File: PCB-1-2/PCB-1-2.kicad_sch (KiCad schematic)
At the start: 79 parts, among them J1 Bus_PCI_Express_x8, J2 ST STDC14 (Debug Connector), J3 USB4105-GF-A, U1 LTC1298IS8_PBF, U10 INA827AIDGKR, U11 LTC1250CS8-PBF, U12 REF3425MDBVTEP, U13 HI-3585APQI, U2 LTC1451IS8-PBF, U3 HI-3110PSIF, U4 FT231XS-R, U5 STM32F103RBT6, U6 STWD100YNXWY3F, U7 ADP7104ACPZ-R7 (v3.3), U8 OPA2187IDGKR, U9 ADP7104ACPZ-R7 (5v), Y1 8MHz Crystal

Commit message: Moved a few things around and shrunk the overall schematic size
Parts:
- removed D1, D2: LED, symbol Device:LED
- removed R11, R12: R, symbol Device:R
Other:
- moved on the sheet: U3

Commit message: Updated Schematic & organized the board layout
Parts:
- added C32, C35, C36: 47uF, Capacitor_SMD:C_0805_2012Metric, symbol Device:C
- added C33, C34, C37, C38: 0.1uF, Capacitor_SMD:C_0805_2012Metric, symbol Device:C
- added C39, C44: .001uF, Capacitor_SMD:C_0805_2012Metric, symbol Device:C
- added C40, C43: .01uF, Capacitor_SMD:C_0805_2012Metric, symbol Device:C
- added C41, C42: .1uF, Capacitor_SMD:C_0805_2012Metric, symbol Device:C
- added C45, C46: 10pF, Capacitor_SMD:C_0805_2012Metric, symbol Device:C
- added D1: PWR_LED, LED_SMD:LED_0805_2012Metric, symbol Device:LED
- added R1, R29: 22, Resistor_SMD:R_0805_2012Metric, symbol Device:R
- added R11: 10k, Resistor_SMD:R_0805_2012Metric, symbol Device:R
- added R12: 1.5Meg, Resistor_SMD:R_0805_2012Metric, symbol Device:R
- added R27: 4.7k, Resistor_SMD:R_0805_2012Metric, symbol Device:R
- added R28: 2k, Resistor_SMD:R_0805_2012Metric, symbol Device:R
- added Y2: ABM8-24.000MHz-10-B1U-T, SDII LIB:XTAL_ABM8-24.000MHz-10-B1U-T, symbol ABM8-24MHz (Crystal):ABM8-24.000MHz-10-B1U-T
- C21, C22, C23, C24, C25, C26, C27, C28, C29, C30, C31: footprint (none) -> Capacitor_SMD:C_0805_2012Metric
- FB2: footprint (none) -> Inductor_SMD:L_0805_2012Metric
- R13, R14, R15, R16, R17, R18, R19, R2, R20, R21, R22, R23, R24, R25, R26, R3, R4: footprint (none) -> Resistor_SMD:R_0805_2012Metric
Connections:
- net SPI2_CS is gone; now on net SPI1_CS: U1.1 (*CS/SHDN), U13.9 (~{CS}), U2.3 (*CS/LD), U5.33 (PB12)
- net +3.3V: now also C32.1, C33.1, C38.2, C42.2, C43.2, C44.2, R11.1, R28.1
- net +5V: now also C34.1, C35.1, C39.1, C40.1, C41.1
- net -5V: now also C36.2, C37.2
- net GND: now also C27.2, J3.SH1 (SHELL_GND), J3.SH2 (SHELL_GND__1), J3.SH3 (SHELL_GND__2), J3.SH4 (SHELL_GND__3), C32.2, C33.2, C34.2, C35.2, C36.1, C37.1, C38.1, C39.2, C40.2, C41.2, C42.1, C43.1, C44.1, C45.2, C46.2, D1.1 (K), R1.2, Y2.2 (GND), Y2.4 (GND__1); no longer U13.17 (GND)
- net MCU_NRST: now also R27.1; no longer U6.1 (*WDO)
- net SPI1_CS: now also U3.16 (*CS)
- net SPI1_MISO: now also U3.15 (SO)
- net SPI1_MOSI: now also U3.14 (SI)
- net SPI1_SCK: now also U3.13 (SCK)
- net SWCLK: now also R29.2; no longer J2.06 (SWCLK)
- net 429_RFLAG: now reaches U5.29 (PB10)
- net 429_RFLAG: now also U13.25 (RFLAG)
- net 429_TFLAG: now reaches U5.30 (PB11)
- net 429_TFLAG: now also U13.28 (TFLAG)
- net 429_MR: now reaches U5.53 (PC12)
- net 429_MR: now also U13.7 (MR)
- net 825_INT: now reaches U5.56 (PB4)
- net 825_INT: now also U3.18 (INT)
- net 825_MR: now reaches U5.57 (PB5)
- net 825_MR: now also U3.17 (MR), R11.2
- net 825_GP1: now reaches U5.58 (PB6)
- net 825_GP1: now also U3.4 (GP1)
- net 825_GP2: now reaches U5.59 (PB7)
- net 825_GP2: now also U3.5 (GP2)
- net 825_TXEN: now reaches U5.61 (PB8)
- net 825_TXEN: now also U3.6 (TXEN)
- net 825_STAT: now reaches U5.62 (PB9)
- net 825_STAT: now also U3.12 (STAT)
- net 825_CANH: now reaches U3.10 (CANH)
- net at U3.2 (OSCOUT): now also C45.1, R12.1, Y2.1
- net at U3.3 (OSCIN): now also C46.1, R12.2, Y2.3
- net 825_CANL: now reaches U3.9 (CANL)
- new net: R27.2, U6.1 (*WDO)
- new net: D1.2 (A), R28.2
- new net: J2.06 (SWCLK), R29.1
- new net: R1.1, U13.17 (GND)
- no-connect marks 23 -> 21
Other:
- note added: "Do we need a 60 Ohm resistor between CANH-SPLIT and CANL-SPLIT? or is it internal? {See HI3110-45}"
- note added: "HI-3110 (ARINC 825)"
- note removed: "Add these if there are extra pins go high when TX and RX buffer are empty)"
- note removed: "Master Reset (ADD IF EXTRA PINS)"
- moved on the sheet: J1, U3

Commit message: Added -5v Inverter
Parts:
- added C47, C50: .1uF, symbol Device:C
- added C49: 68uF, symbol Device:C
- added C51: 120uF, symbol Device:C
- added D2: 1N5817, symbol Device:D
- added L2: 47uH, symbol Device:L
- added R30, R31: 60, symbol Device:R
- added U14: MAX764ESA, SDII LIB:SO-G8_1_MXM, symbol MAX764ESA (-5v Inverter):MAX764ESA
- C18, C19: value 4.7uF -> 22uF
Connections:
- net +5V: now also C50.1, C51.1, U14.6 (V+), U14.7 (V+)
- net -5V: now also C49.1, D2.2 (A), U14.1 (OUT)
- net 825_CANH: now also R31.1
- net 825_CANL: now also R30.1
- net GND: now also C47.2, C49.2, C50.2, C51.2, L2.1, U14.3 (SHDN), U14.5 (GND)
- net at U3.7 (SPLIT): now also R30.2, R31.2
- new net: C47.1, U14.2 (FB), U14.4 (REF)
- new net: D2.1 (K), L2.2, U14.8 (LX)
- no-connect marks 21 -> 20
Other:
- note added: "MAX764ESA (-5v Inverter)"
- note added: "PCIE-x8 Connector"
- note added: "STM32F103RB (MCU)"
- note added: "Team ACDC"
- moved on the sheet: C10, C11, C12, C13, C14, C15, C16, C17, C20, C39, C40, C41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

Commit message: Hopefully completed schematic
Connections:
- net +5V: now also C2.1, U2.8 (VCC)
- net SPI1_CS: no longer U1.1 (*CS/SHDN), U13.9 (~{CS}), U2.3 (*CS/LD), U5.33 (PB12)
- net SPI2_CLK: no longer U5.34 (PB13)
- net SPI2_SCK: now also U5.34 (PB13)
- new net SPI2_CS: U1.1 (*CS/SHDN), U13.9 (~{CS}), U2.3 (*CS/LD), U5.33 (PB12)
- no-connect marks 20 -> 28
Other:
- note added: "429_IN+ & 429_IN- are both optional"
- note added: "V+_FROM_PCIE should be the 7-ish volts"

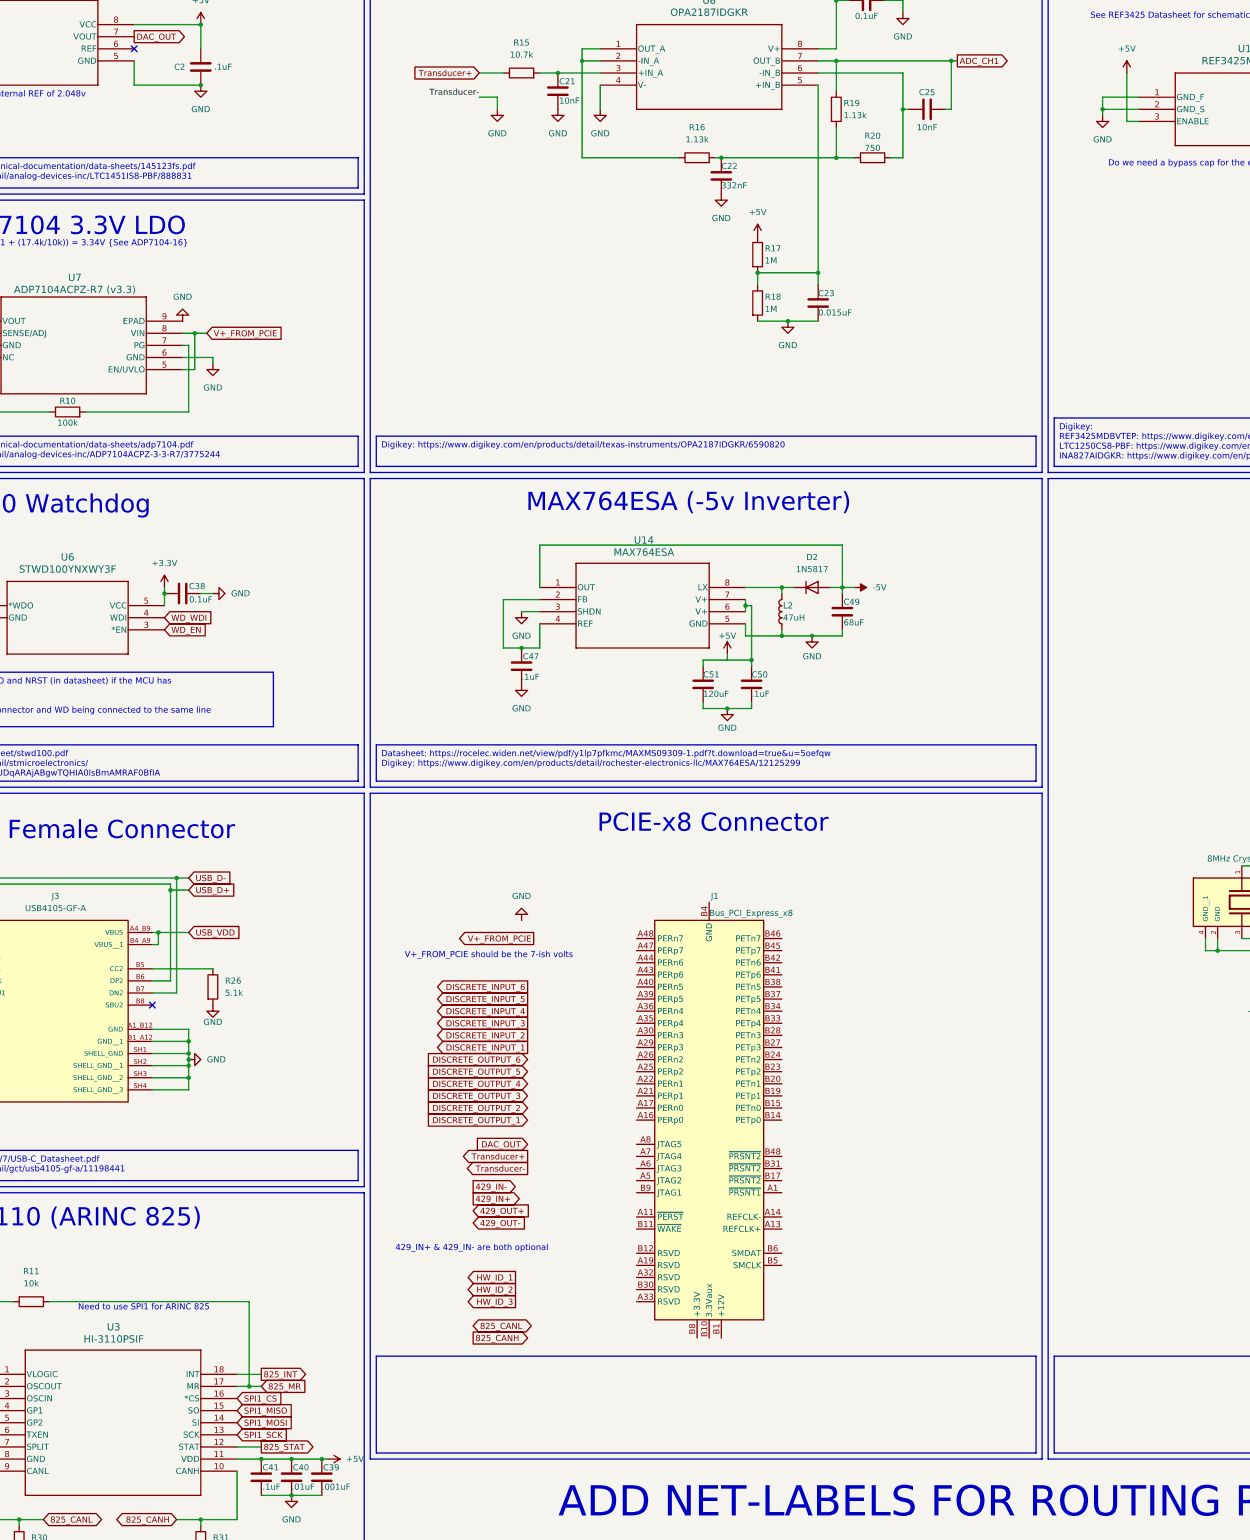
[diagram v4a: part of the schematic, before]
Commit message: Fixing PCIe simple, not done yet
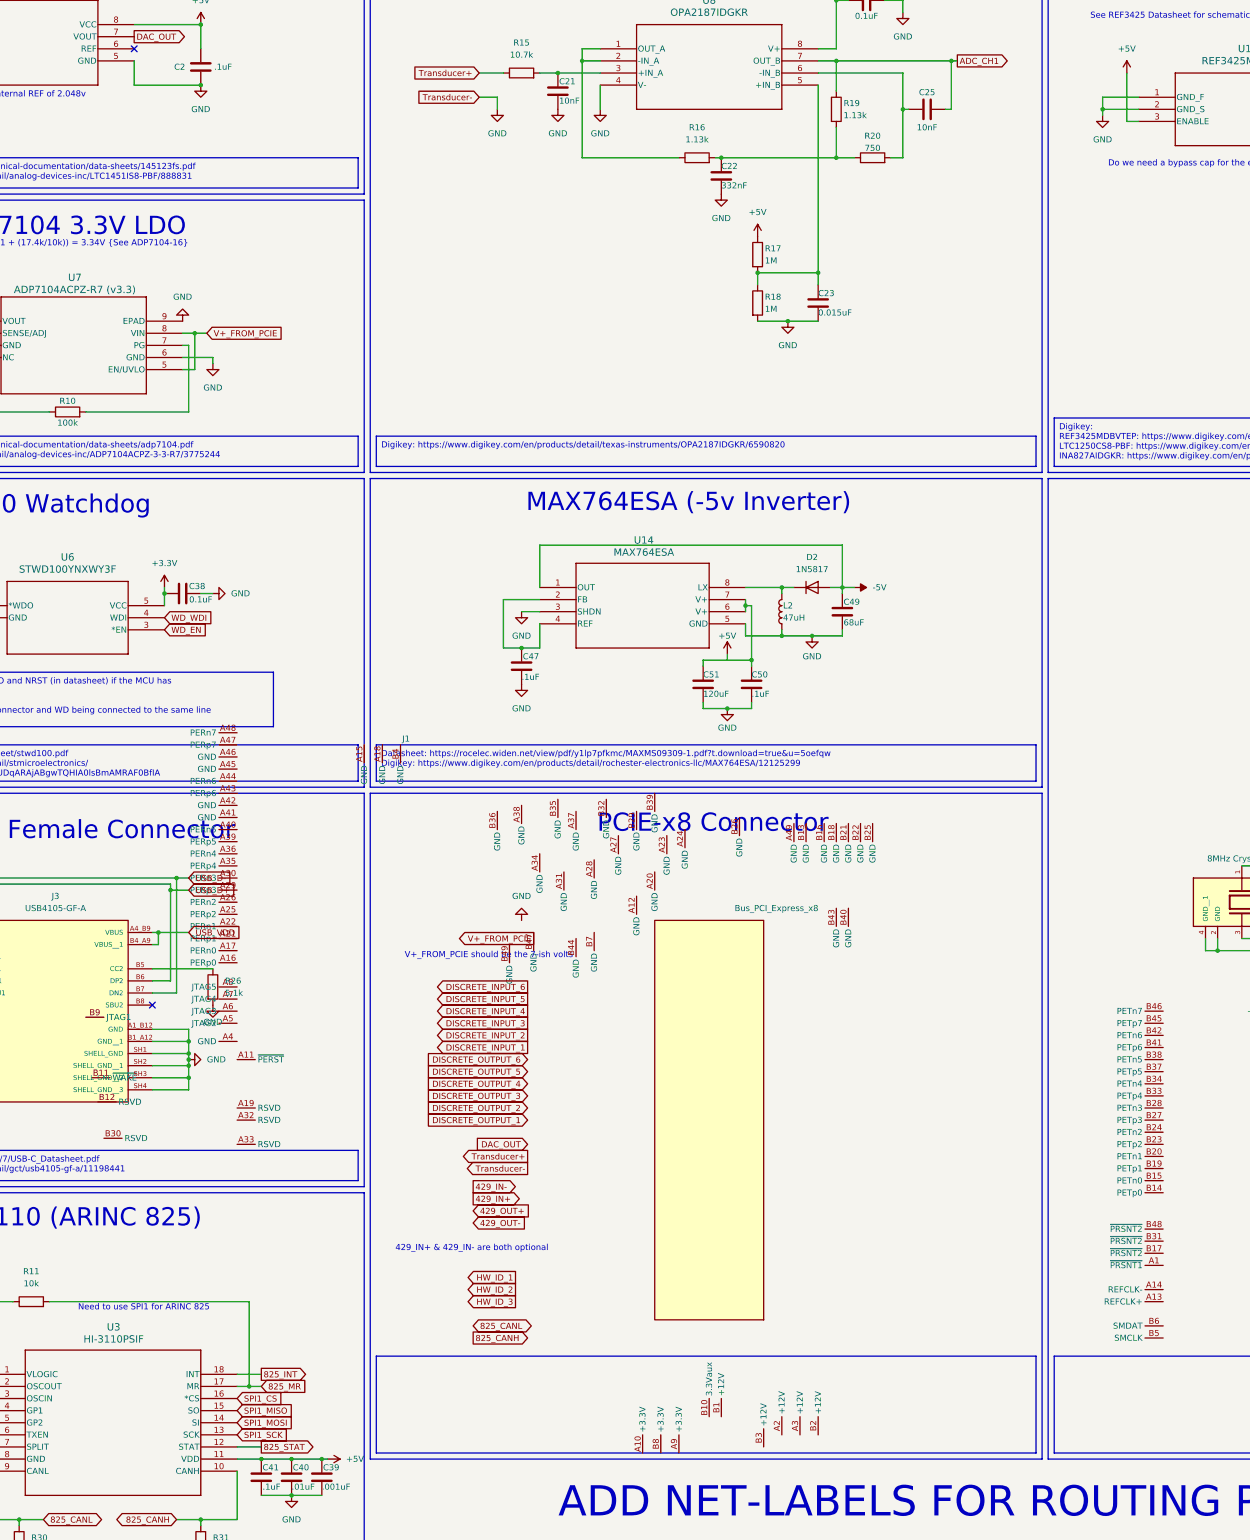
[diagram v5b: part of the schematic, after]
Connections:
- now unconnected: J1.A10 (+3.3V), J1.A12 (GND), J1.A15 (GND), J1.A18 (GND), J1.A2 (+12V), J1.A20 (GND), J1.A23 (GND), J1.A24 (GND), J1.A27 (GND), J1.A28 (GND), J1.A3 (+12V), J1.A31 (GND), J1.A34 (GND), J1.A37 (GND), J1.A38 (GND), J1.A4 (GND), J1.A41 (GND), J1.A42 (GND), J1.A45 (GND), J1.A46 (GND), J1.A49 (GND), J1.A9 (+3.3V), J1.B1 (+12V), J1.B13 (GND), J1.B16 (GND), J1.B18 (GND), J1.B2 (+12V), J1.B21 (GND), J1.B22 (GND), J1.B25 (GND), J1.B26 (GND), J1.B29 (GND), J1.B3 (+12V), J1.B32 (GND), J1.B35 (GND), J1.B36 (GND), J1.B39 (GND), J1.B4 (GND), J1.B40 (GND), J1.B43 (GND), J1.B44 (GND), J1.B47 (GND), J1.B49 (GND), J1.B7 (GND), J1.B8 (+3.3V)
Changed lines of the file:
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@@
 		)
 	)
-	(label "Transducer-"
-		(at 284.48 59.69 180)
-		(fields_autoplaced yes)
-		(effects
-			(font
-				(size 1.27 1.27)
-			)
-			(justify right bottom)
-		)
-	)
 	(label "ADC_CH0"
 		(at 39.37 45.72 0)
@@
 		)
 	)
+	(global_label "Transducer-"
+		(shape input)
+		(at 284.48 59.69 180)
+		(fields_autoplaced yes)
+		(effects
+			(font
+				(size 1.27 1.27)
+			)
+			(justify right)
+		)
+		(property "Intersheetrefs" "${INTERSHEET_REFS}"
+			(at 269.5811 59.69 0)
+			(effects
+				(font
+					(size 1.27 1.27)
+				)
+				(justify right)
+				(hide yes)
+			)
+		)
+	)
 	(global_label "SPI2_CS"
 		(shape input)
@@
 		(dnp no)
 		(property "Reference" "J1"
-			(at 333.0859 227.33 0)
+			(at 268.3159 194.31 0)
 			(effects
 				(font
@@
 		)
 		(property "Value" "Bus_PCI_Express_x8"
-			(at 332.74 230.886 0)
+			(at 338.074 229.87 0)
 			(effects
 				(font
@@
 		)
 		(property "Footprint" "Connector_PCBEdge:BUS_PCIexpress_x8"
-			(at 332.74 279.4 0)
+			(at 262.128 256.032 0)
 			(effects
 				(font
@@
 		)
 		(property "Datasheet" "http://www.ritrontek.com/uploadfile/2016/1026/20161026105231124.pdf#page=63"
-			(at 334.01 250.19 0)
+			(at 258.826 293.116 0)
 			(effects
 				(font
@@
 		)
 		(property "Description" "PCI Express bus connector x8"
-			(at 332.74 274.32 0)
+			(at 268.224 251.714 0)
 			(effects
 				(font

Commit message: Merged both -1/-2 and backplane
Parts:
- added C48, C52, C54, C59, C60, C61, C62: 22uF, Capacitor_SMD:C_0805_2012Metric, symbol Device:C
- added C53: 2.2uF, Capacitor_SMD:C_0805_2012Metric, symbol Device:C
- added C55: 200pF, Capacitor_SMD:C_0603_1608Metric, symbol Device:C
- added C56, C57: 20pF, Capacitor_SMD:C_0805_2012Metric, symbol Device:C
- added C58: 330nF, Capacitor_SMD:C_0805_2012Metric, symbol Device:C
- added D5: GPIO_LED, LED_SMD:LED_0805_2012Metric, symbol Device:LED
- added H1, H2, H3, H4: MountingHole, MountingHole:MountingHole_2.2mm_M2, symbol Mechanical:MountingHole
- added J4: Conn_01x02_Pin, SDII LIB:pin header, symbol Connector:Conn_01x02_Pin
- added R28: 1.2k, Resistor_SMD:R_0805_2012Metric, symbol Device:R
- added R32, R33: 30, Resistor_SMD:R_0603_1608Metric, symbol Device:R
- C22: value 332nF -> 2nF; footprint Capacitor_SMD:C_0805_2012Metric -> Capacitor_SMD:C_0603_1608Metric
- C23: footprint Capacitor_SMD:C_0805_2012Metric -> Capacitor_SMD:C_0402_1005Metric
- C29: value 400pF -> 200pF; footprint Capacitor_SMD:C_0805_2012Metric -> Capacitor_SMD:C_0603_1608Metric
- C30, C31: value 40pF -> 20pF
- C47, C50: footprint (none) -> Capacitor_SMD:C_0603_1608Metric
- C49: value 68uF -> 22uF; footprint (none) -> Capacitor_SMD:C_0805_2012Metric
- C51: value 120uF -> 10uF; footprint (none) -> Capacitor_SMD:C_1206_3216Metric
- D2: footprint (none) -> SDII LIB:1N5817
- D3, D4, L2: footprint (none) -> LED_SMD:LED_0805_2012Metric
- FB1: value FerriteBead -> 120R; footprint (none) -> Inductor_SMD:L_0805_2012Metric
- R30, R31: value 60 -> 30; footprint (none) -> Resistor_SMD:R_0603_1608Metric
- R34: renamed from R28; value 2k -> 1.2k
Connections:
- net +3.3V: no longer C13.1, C14.1, FB2.1, U5.13 (VDDA)
- net +5V: now also R5.2, C54.1, C59.1, C60.1, C61.1, C62.1; no longer R5.1
- net -5V: now also C48.1, C52.1, C53.1
- net 429_IN+: now also J1.A11 (A429_In+)
- net 429_IN-: now also J1.A10 (A429_In-)
- net 429_MR: now also U5.45 (PA12); no longer U5.53 (PC12)
- net 429_OUT+: now also J1.A12 (A429_Out-)
- net 429_OUT-: now also J1.A13 (A429_OUT+)
- net 429_RFLAG: now also U5.40 (PC9); no longer U5.29 (PB10)
- net 429_TFLAG: now also U5.41 (PA8); no longer U5.30 (PB11)
- net 825_CANH: now also J1.A8 (CANLO), J4.2 (Pin_2)
- net 825_CANL: now also J1.A7 (CANHI), J4.1 (Pin_1)
- net 825_GP2: now also U5.57 (PB5); no longer U5.59 (PB7)
- net 825_MR: now also U5.55 (PB3); no longer U5.57 (PB5)
- net 825_STAT: now also U5.53 (PC12); no longer U5.62 (PB9)
- net 825_TXEN: now also U5.54 (PD2); no longer U5.61 (PB8)
- net ARINC_429_CLK: now also U5.44 (PA11); no longer U5.26 (PB0)
- net DAC_OUT: now also J1.A5 (DAC)
- net DISCRETE_INPUT_1: now also J1.A19 (DI1), U5.30 (PB11); no longer U5.37 (PC6)
- net DISCRETE_INPUT_2: now also J1.A20 (DI2), U5.29 (PB10); no longer U5.38 (PC7)
- net DISCRETE_INPUT_3: now also J1.A21 (DI3), U5.28 (PB2); no longer U5.39 (PC8)
- net DISCRETE_INPUT_4: now also J1.A22 (DI4), U5.27 (PB1); no longer U5.40 (PC9)
- net DISCRETE_INPUT_5: now also J1.A23 (DI5), U5.26 (PB0); no longer U5.51 (PC10)
- net DISCRETE_INPUT_6: now also J1.A24 (DI6), U5.25 (PC5); no longer U5.52 (PC11)
- net DISCRETE_OUTPUT_1: now also J1.A27 (DO1), U5.15 (PA1); no longer U5.8 (PC0)
- net DISCRETE_OUTPUT_2: now also J1.A28 (DO2), U5.14 (PA0-WKUP); no longer U5.9 (PC1)
- net DISCRETE_OUTPUT_3: now also J1.A29 (DO3), U5.11 (PC3); no longer U5.10 (PC2)
- net DISCRETE_OUTPUT_4: now also J1.A30 (DO4), U5.10 (PC2); no longer U5.11 (PC3)
- net DISCRETE_OUTPUT_5: now also J1.A31 (DO5), U5.9 (PC1); no longer U5.24 (PC4)
- net DISCRETE_OUTPUT_6: now also J1.A32 (DO6), U5.8 (PC0); no longer U5.25 (PC5)
- net GND: now also J1.A16 (GND), J1.A18 (GND), J1.A25 (GND), J1.A26 (GND), J1.A33 (GND), J1.A6 (GND), J1.A9 (GND), J1.B4 (GND), C48.2, C52.2, C53.2, C54.2, C56.2, C57.2, C58.2, C59.2, C60.2, C61.2, C62.2, D5.1 (K)
- net HW_ID_1: now also J1.A34 (Resistor), U5.62 (PB9); no longer U5.27 (PB1)
- net HW_ID_2: now also J1.A35 (Resistor), U5.61 (PB8); no longer U5.28 (PB2)
- net HW_ID_3: now also J1.A36 (Resistor), U5.59 (PB7); no longer U5.55 (PB3)
- net RTD+: now also J1.A4 (RTD_+)
- net RTD-: now also J1.A3 (RTD_-)
- net Transducer+: now also J1.A2 (TD+)
- net V+_FROM_PCIE: now also J1.A17 (Power_Input)
- net WD_EN: now also U5.51 (PC10); no longer U5.15 (PA1)
- net WD_WDI: now also U5.52 (PC11); no longer U5.14 (PA0-WKUP)
- net at U9.7 (PG): now also R5.1; no longer R5.2
- net at C29.1, C30.1, R22.2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: now also C55.1, C57.1
- net at C29.2, C31.1, R23.2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: now also C55.2, C56.1
- net at C22.1, R16.2, R19.2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: now also C58.1
- net NC: now reaches J1.B1 (NC)
- net NC: now also J1.B10 (NC), J1.B8 (NC)
- new net: R28.1, U5.37 (PC6)
- new net: R31.2, R33.1
- new net: R32.2, R33.2, U3.7 (SPLIT)
- new net: R30.2, R32.1
- new net: D5.2 (A), R28.2
- new net +3.3VA: C13.1, C14.1, FB2.1, U5.13 (VDDA)
- no-connect marks 28 -> 23
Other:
- note added: "Going to ground the tranducer - pin on the backplane as the schematic is being weird if I do not"
- note added: "Swap WDI, WEN and O5/O6"
- note added: "Text devin to add LED after routing"
- moved on the sheet: C22, C29, C30, C31, C51, R16, R21, R22, R23, R31, R5, R6

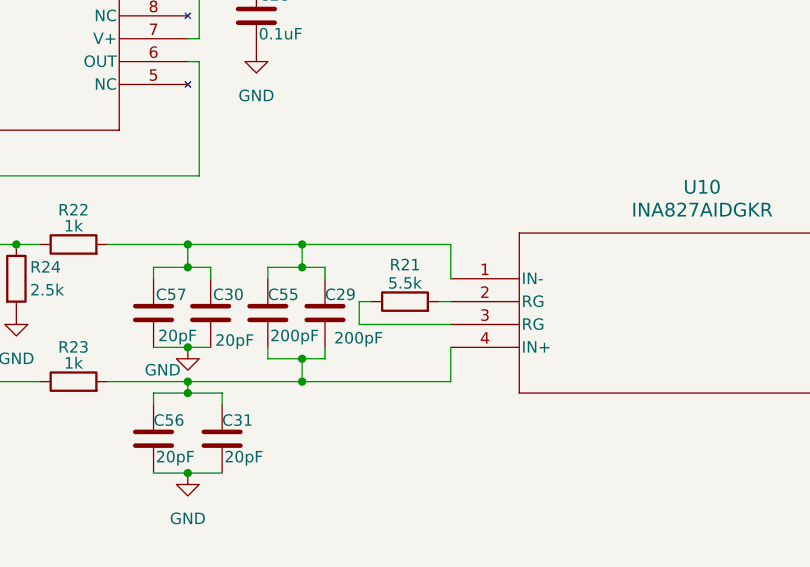
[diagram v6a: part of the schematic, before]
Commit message: Generated PCB BOM & CSV
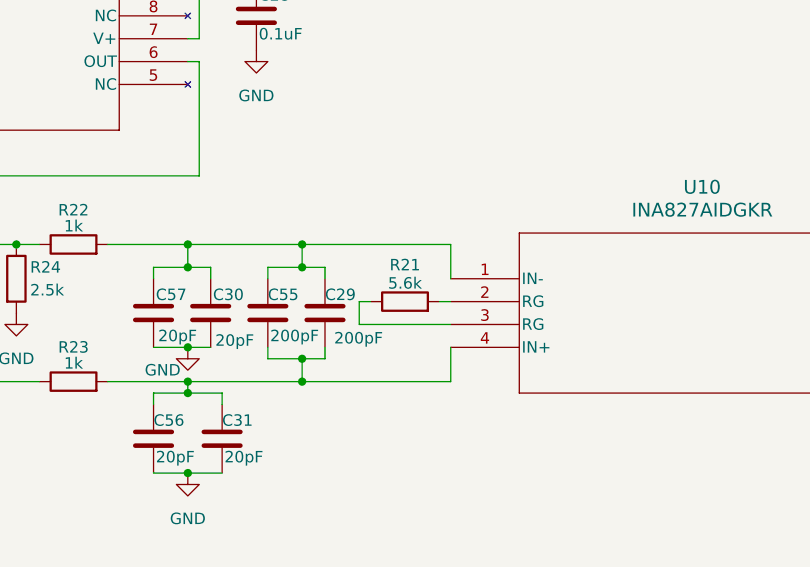
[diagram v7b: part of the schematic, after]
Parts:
- L2: footprint LED_SMD:LED_0805_2012Metric -> Inductor_SMD:L_0805_2012Metric
- R21: value 5.5k -> 5.6k
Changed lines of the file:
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@@
 			)
 		)
-		(property "Value" "5.5k"
+		(property "Value" "5.6k"
 			(at 553.72 84.328 90)
 			(effects
@@
 			)
 		)
-		(property "Footprint" "LED_SMD:LED_0805_2012Metric"
+		(property "Footprint" "Inductor_SMD:L_0805_2012Metric"
 			(at 347.98 167.64 0)
 			(effects
